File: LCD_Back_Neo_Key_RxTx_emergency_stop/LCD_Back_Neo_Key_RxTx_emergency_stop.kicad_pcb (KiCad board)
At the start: 2 copper layers, 109.7 x 102.1 mm, 27 parts, among them J1 Screw_Terminal_01x14, J2 Conn_01x20_Female, J3 Conn_01x08_Male_KeyPad, J4 Display_support_pin, J5 Display_support_pin, K1 FINDER-34.51, K2 FINDER-34.51, K3 FINDER-34.51, K4 FINDER-34.51, Q1 BC337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

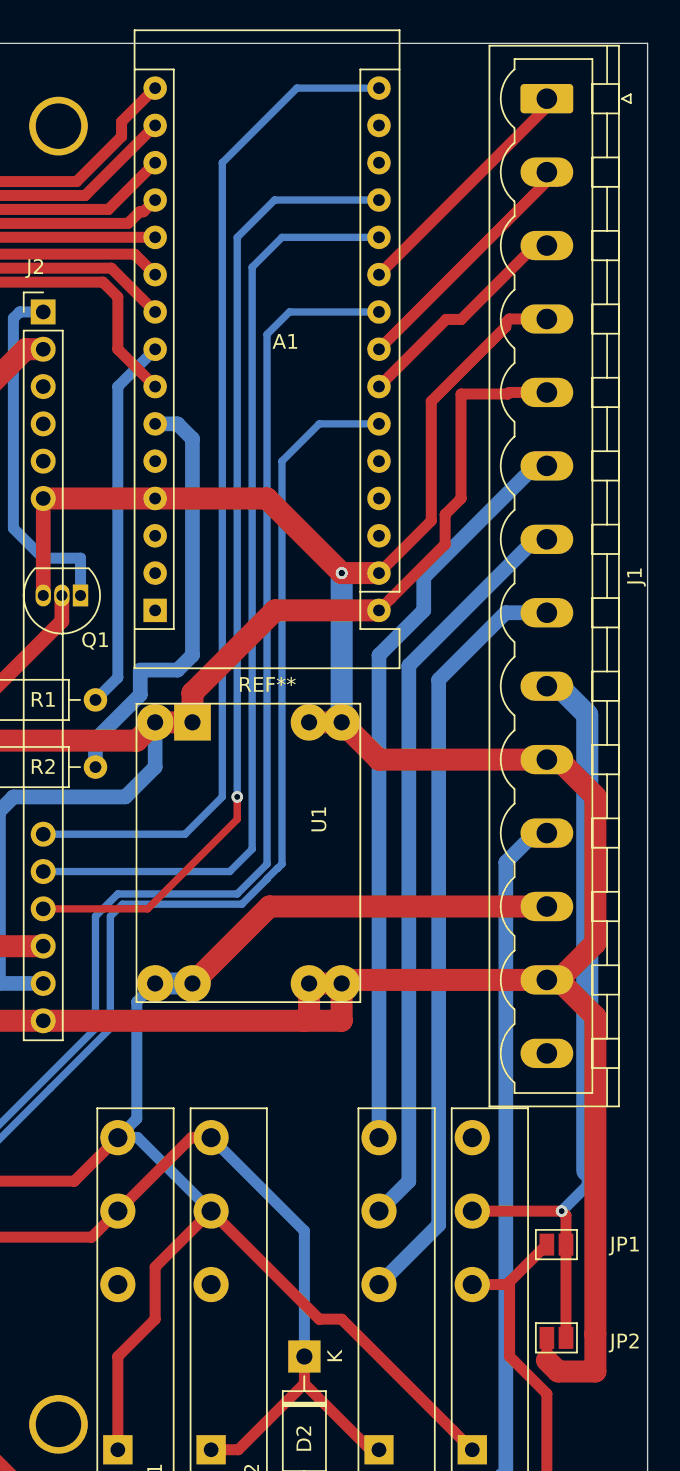
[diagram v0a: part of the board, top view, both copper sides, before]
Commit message: remove all through-connection. Manufacturer can't handle
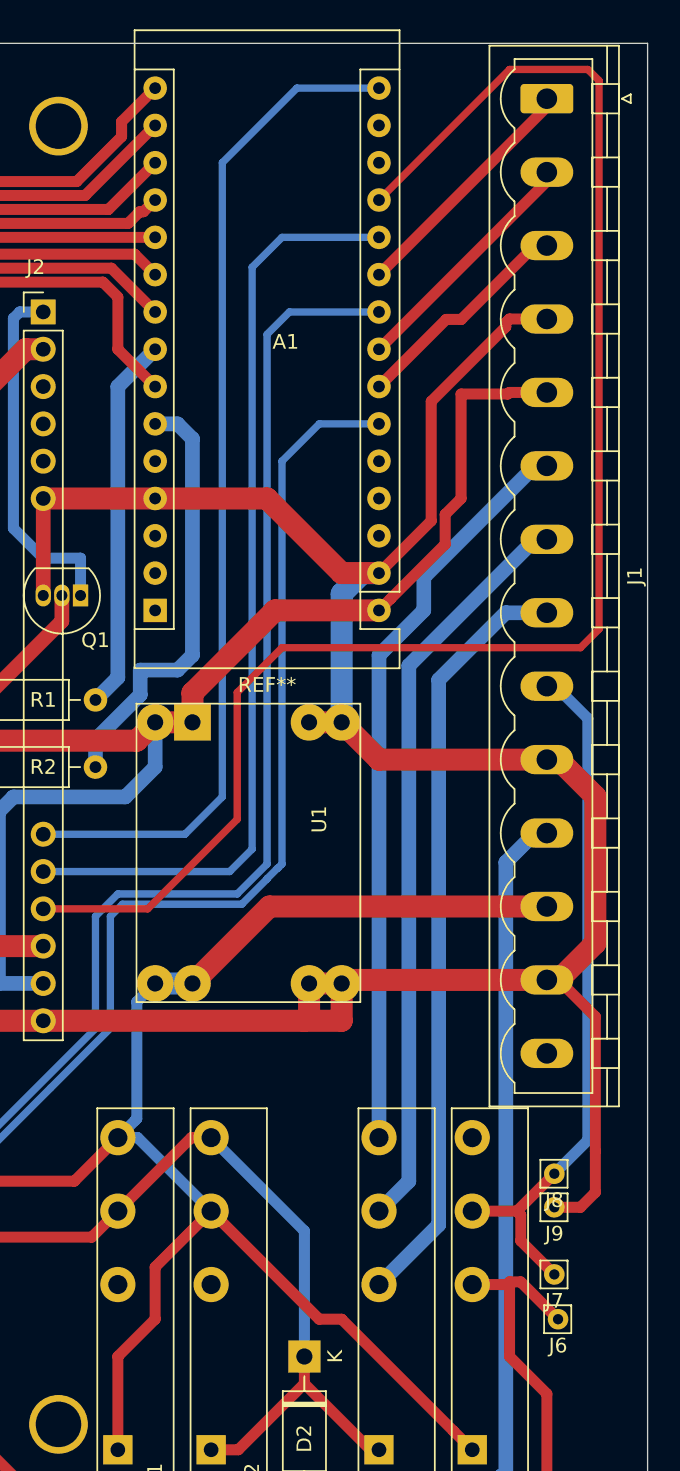
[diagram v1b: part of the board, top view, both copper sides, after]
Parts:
- removed JP1, JP2: Jumper_lon-jumper_lon, Jumper:SolderJumper-2_P1.3mm_Open_Pad1.0x1.5mm
- added J6: Jumper1, Connector_Pin:Pin_D0.7mm_L6.5mm_W1.8mm_FlatFork, F.Cu at (207.8, 119.4)
- added J7: Jumper 1, Connector_Pin:Pin_D0.7mm_L6.5mm_W1.8mm_FlatFork, F.Cu at (207.5, 116.3)
- added J8: Jumper2, Connector_Pin:Pin_D0.7mm_L6.5mm_W1.8mm_FlatFork, F.Cu at (207.5, 109.5)
- added J9: Jumper 2, Connector_Pin:Pin_D0.7mm_L6.5mm_W1.8mm_FlatFork, F.Cu at (207.5, 111.8)
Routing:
- net Ardu_A0: track 66.1 -> 107.1 mm, vias 1 -> 0
- net GND: track 243.0 -> 230.6 mm, vias 2 -> 0
- net ScrewTerm11-EmergencyStopSwitch1: track 52.9 -> 48.5 mm, vias 1 -> 0
- net Net-(D2-Pad2): track 47.4 -> 48.2 mm

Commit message: grow up Pads
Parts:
- moved J7 0.92 mm to (208.3, 116.8)
- moved J8 0.80 mm to (208.3, 109.2)
- moved J9 0.76 mm to (208.3, 111.8)
- moved J6 0.51 mm to (208.3, 119.4)
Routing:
- net GND: track 230.6 -> 229.9 mm
- net Ardu_A0: track 107.1 -> 107.7 mm

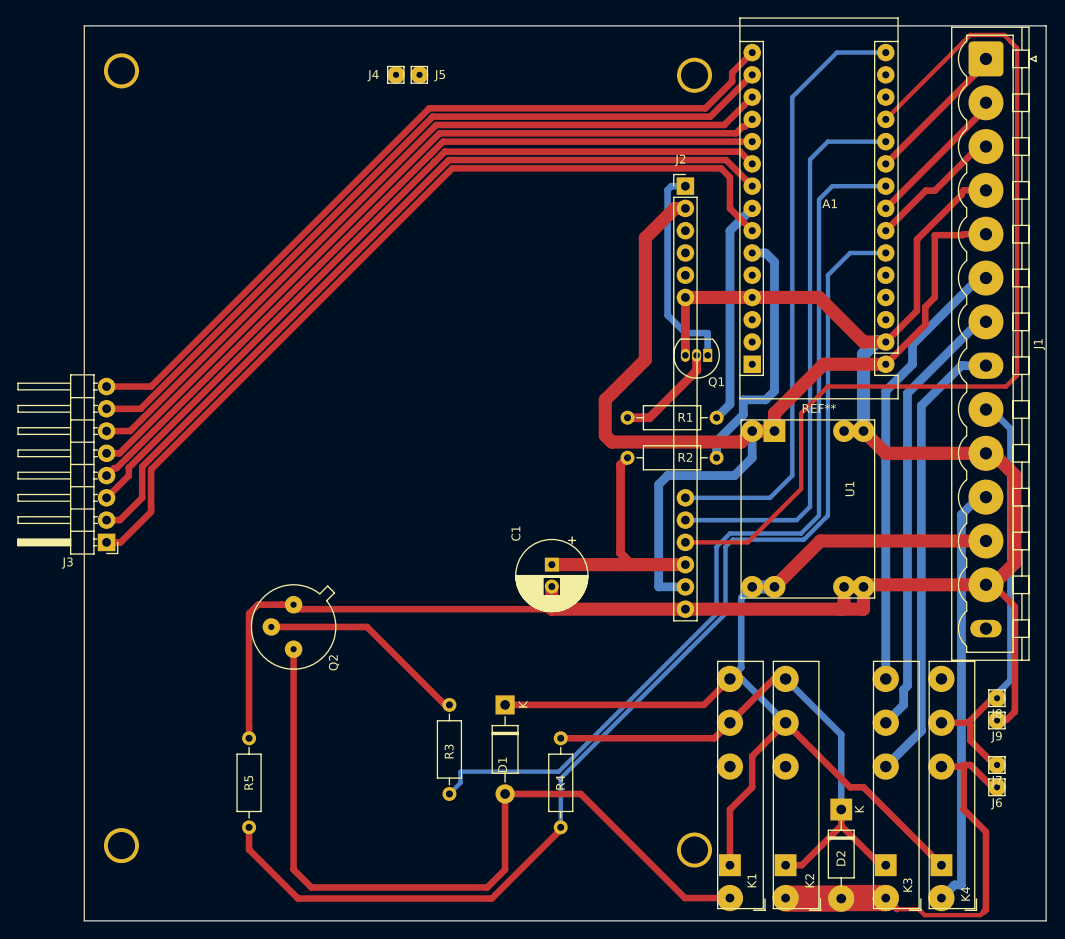
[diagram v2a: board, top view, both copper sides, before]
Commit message: remove screw holes
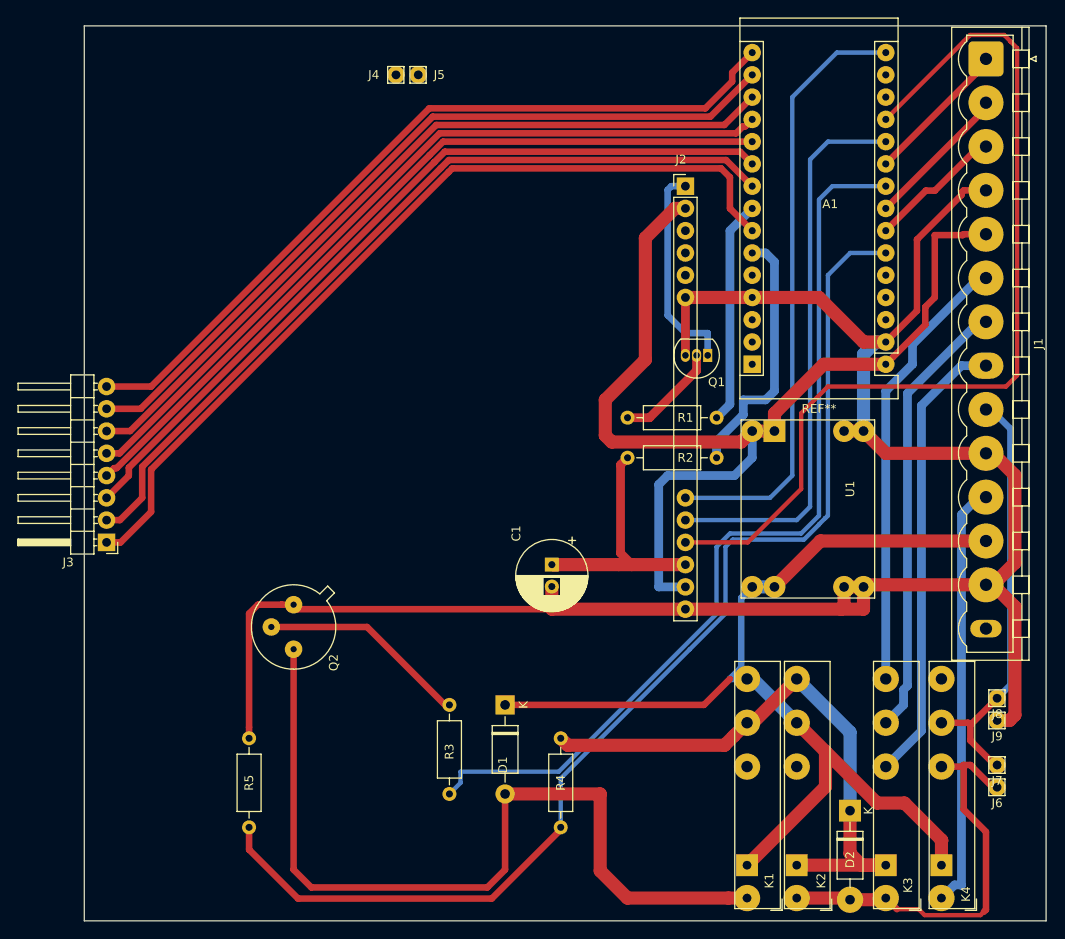
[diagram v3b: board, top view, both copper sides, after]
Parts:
- removed  : , Socket_Arduino_Micro:1pin_Micro (x4)
- moved K1 1.95 mm to (179.8, 128.3)
- moved K2 1.27 mm to (185.4, 128.3)
- moved D2 1.01 mm to (191.5, 122.0)
- moved J5 0.15 mm to (142.2, 38.1)
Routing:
- net Net-(D1-Pad2): track 90.2 -> 97.3 mm
- net Net-(D2-Pad1): track 63.0 -> 68.2 mm
- net VCC-24V: track 119.1 -> 118.0 mm
- net Net-(D2-Pad2): track 48.5 -> 47.4 mm
